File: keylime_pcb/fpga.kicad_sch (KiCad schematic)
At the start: 11 parts, among them U1 xc7s15cpga196

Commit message: Testing push again
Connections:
- net GND: now also U1.A1 (GND[54]), U1.A11 (GND[54]), U1.A14 (GND[54]), U1.A6 (GND[54]), U1.B13 (GND[54]), U1.B3 (GND[54]), U1.B8 (GND[54]), U1.C6 (GND[54]), U1.C8 (GND[54]), U1.D12 (GND[54]), U1.D2 (GND[54]), U1.D5 (GND[54]), U1.D7 (GND[54]), U1.D9 (GND[54]), U1.E10 (GND[54]), U1.E14 (GND[54]), U1.E4 (GND[54]), U1.E6 (GND[54]), U1.E8 (GND[54]), U1.F1 (GND[54]), U1.F11 (GND[54]), U1.F5 (GND[54]), U1.F9 (GND[54]), U1.G10 (GND[54]), U1.G11 (GND[54]), U1.G13 (GND[54]), U1.G3 (GND[54]), U1.G6 (GND[54]), U1.H5 (GND[54]), U1.H9 (GND[54]), U1.J10 (GND[54]), U1.J12 (GND[54]), U1.J2 (GND[54]), U1.J6 (GND[54]), U1.K14 (GND[54]), U1.K4 (GND[54]), U1.K5 (GND[54]), U1.K7 (GND[54]), U1.K9 (GND[54]), U1.L1 (GND[54]), U1.L11 (GND[54]), U1.L5 (GND[54]), U1.L6 (GND[54]), U1.M13 (GND[54]), U1.M3 (GND[54]), U1.M8 (GND[54]), U1.N10 (GND[54]), U1.N5 (GND[54]), U1.P1 (GND[54]), U1.P14 (GND[54]), U1.P5 (GND[54]), U1.P6 (GND[54]), U1.P7 (GND[54]), U1.P9 (GND[54])
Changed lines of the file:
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@@
+	(wire
+		(pts
+			(xy 196.85 106.68) (xy 217.17 106.68)
+		)
+		(stroke
+			(width 0)
+			(type default)
+		)
+	)
 	(wire
 		(pts
@@
 		(effects
 			(font
+				(size 1.27 1.27)
+			)
+			(justify left bottom)
+		)
+	)
+	(label "GND"
+		(at 196.85 106.68 0)
+		(effects
+			(font

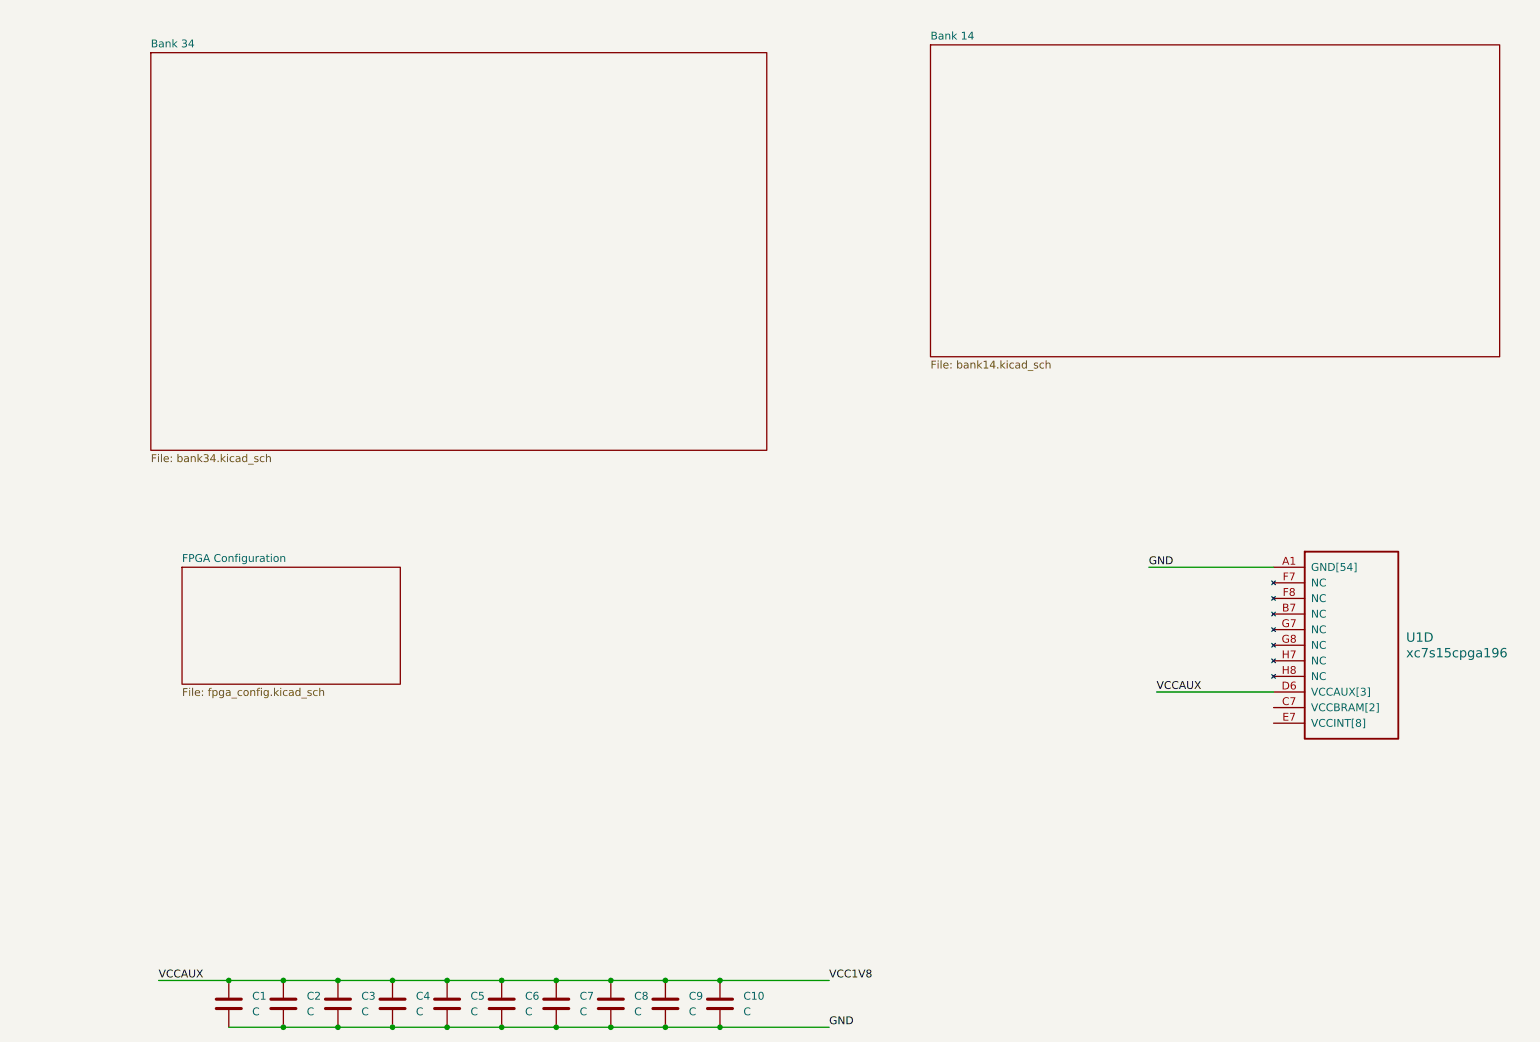
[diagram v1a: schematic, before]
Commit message: Finished adding most components.
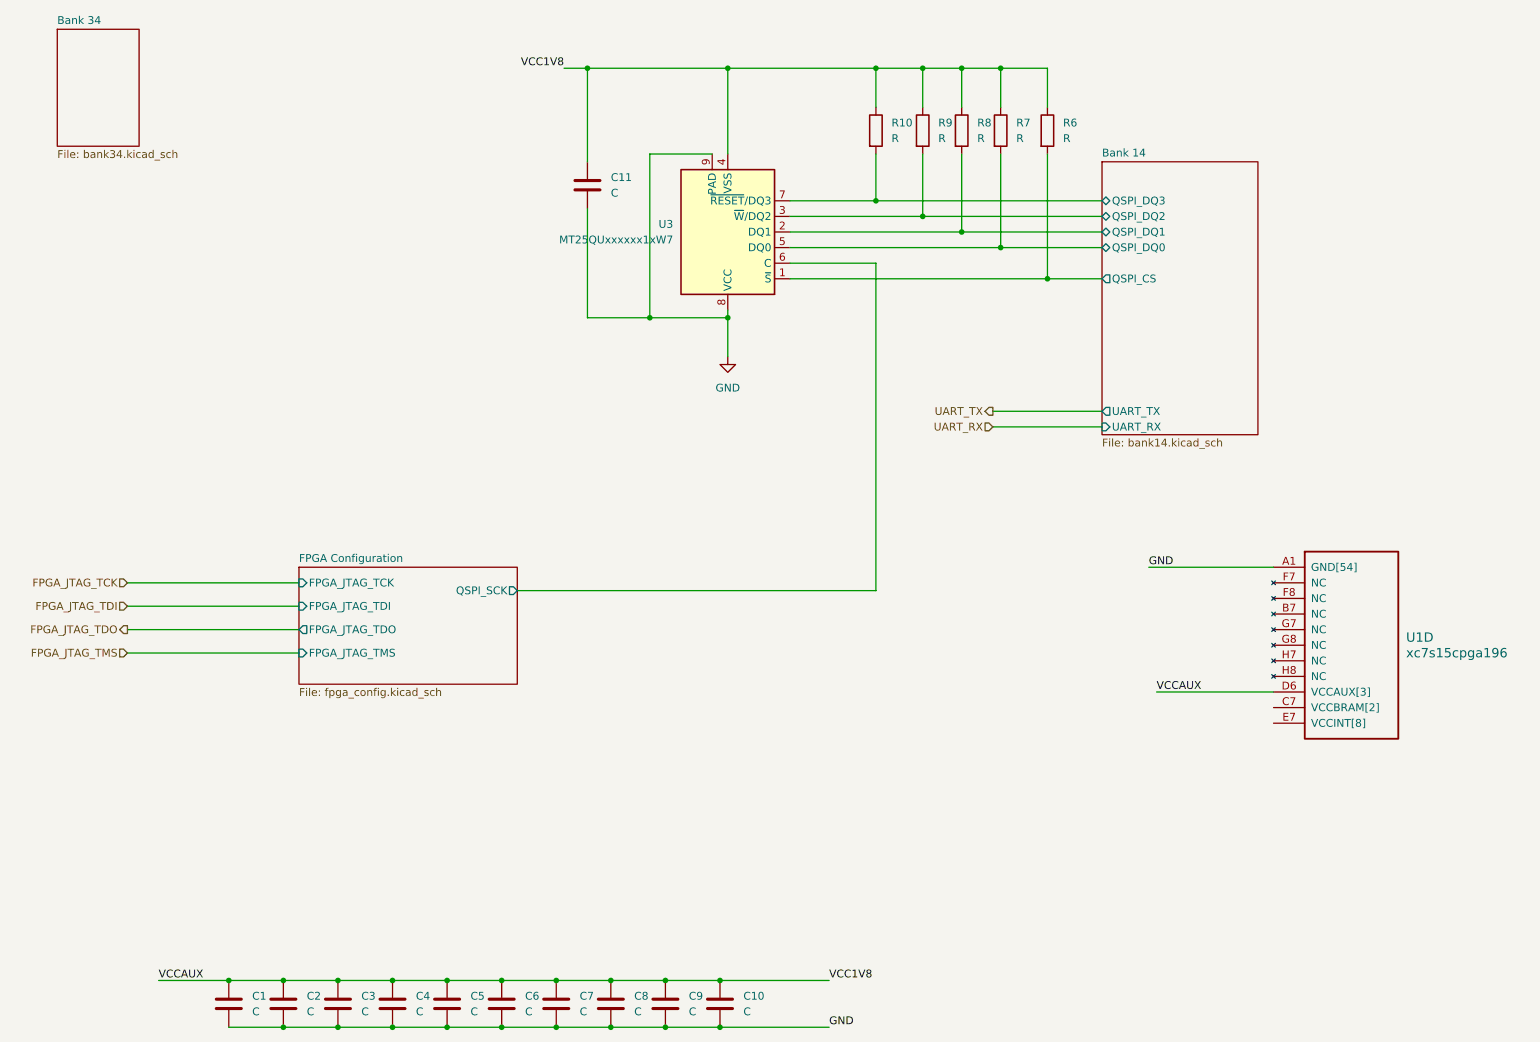
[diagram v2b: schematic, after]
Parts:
- added C11: C, symbol Device:C
- added R10, R6, R7, R8, R9: R, symbol Device:R
- added U3: MT25QUxxxxxx1xW7, Package_DFN_QFN:W-PDFN-8-1EP_6x5mm_P1.27mm_EP3x3mm, symbol Memory_Flash:MT25QUxxxxxx1xW7
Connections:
- net GND: now also C11.2, U3.8 (VCC), U3.9 (PAD)
- net VCC1V8: now also C11.1, R10.1, R6.1, R7.1, R8.1, R9.1, U3.4 (VSS)
- new net Bank 14/QSPI_CS: R6.2, U3.1 (~{S})
- new net Bank 14/QSPI_DQ0: R7.2, U3.5 (DQ0)
- new net Bank 14/QSPI_DQ1: R8.2, U3.2 (DQ1)
- new net Bank 14/QSPI_DQ2: R9.2, U3.3 (~{W}/DQ2)
- new net Bank 14/QSPI_DQ3: R10.2, U3.7 (~{RESET}/DQ3)
- new net FPGA Configuration/QSPI_SCK: U3.6 (C)
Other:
- sheet Bank 14 ports: added QSPI_CS, QSPI_DQ0, QSPI_DQ1, QSPI_DQ2, QSPI_DQ3, UART_RX, UART_TX; removed none
- sheet FPGA Configuration ports: added FPGA_JTAG_TCK, FPGA_JTAG_TDI, FPGA_JTAG_TDO, FPGA_JTAG_TMS, QSPI_SCK; removed none
